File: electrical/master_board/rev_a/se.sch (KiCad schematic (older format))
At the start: 0 parts

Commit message: Added spacer mounting holes to schematics and associated PCB's.
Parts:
- added H3: HOLE;M2.5, MountingHole:MountingHole_2.7mm_M2.5, symbol HR2:HOLE;M2.5
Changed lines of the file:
@@
 Comment4 ""
 $EndDescr
+$Comp
+L HR2:HOLE;M2.5 H3
+U 1 1 5F2F795F
+P 3200 4100
+F 0 "H3" H 3150 4150 60  0000 L CNN
+F 1 "HOLE;M2.5" H 3000 4050 60  0000 L CNN
+F 2 "MountingHole:MountingHole_2.7mm_M2.5" H 3400 4150 60  0001 L CNN
+F 3 "M2.5 Mounting Hole" H 3400 3950 60  0001 L CNN
+	1    3200 4100
+	1    0    0    -1
+$EndComp
 $EndSCHEMATC

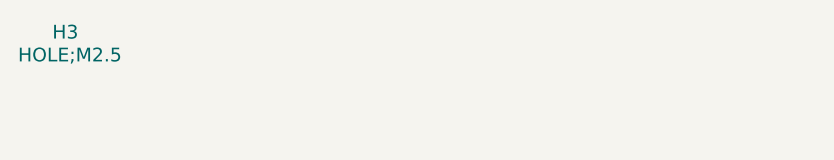
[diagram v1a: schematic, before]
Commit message: Added LED's to the PCB's.
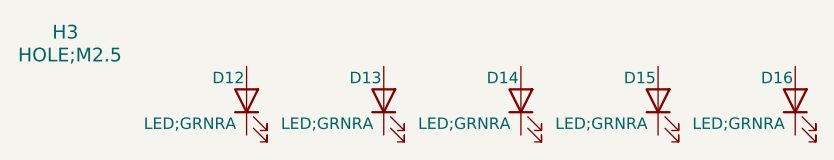
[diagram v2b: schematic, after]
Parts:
- added D12, D13, D14, D15, D16: LED;GRNRA, HR2:LED_GRNRA, symbol Device:LED
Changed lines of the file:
@@
 	1    0    0    -1
 $EndComp
+$Comp
+L Device:LED D12
+U 1 1 5F30C7E5
+P 4000 4350
+F 0 "D12" V 4100 4500 50  0000 R CNN
+F 1 "LED;GRNRA" V 3900 4800 50  0000 R CNN
+F 2 "HR2:LED_GRNRA" H 4000 4350 50  0001 C CNN
+F 3 "~" H 4000 4350 50  0001 C CNN
+	1    4000 4350
+	0    -1   -1   0
+$EndComp
+$Comp
+L Device:LED D14
+U 1 1 5F30E8C7
+P 5200 4350
+F 0 "D14" V 5300 4500 50  0000 R CNN
+F 1 "LED;GRNRA" V 5100 4800 50  0000 R CNN
+F 2 "HR2:LED_GRNRA" H 5200 4350 50  0001 C CNN
+F 3 "~" H 5200 4350 50  0001 C CNN
+	1    5200 4350
+	0    -1   -1   0
+$EndComp
+$Comp
+L Device:LED D15
+U 1 1 5F30E8D1
+P 5800 4350
+F 0 "D15" V 5900 4500 50  0000 R CNN
+F 1 "LED;GRNRA" V 5700 4800 50  0000 R CNN
+F 2 "HR2:LED_GRNRA" H 5800 4350 50  0001 C CNN
+F 3 "~" H 5800 4350 50  0001 C CNN
+	1    5800 4350
+	0    -1   -1   0
+$EndComp
+$Comp
+L Device:LED D16
+U 1 1 5F30F503
+P 6400 4350
+F 0 "D16" V 6500 4500 50  0000 R CNN
+F 1 "LED;GRNRA" V 6300 4800 50  0000 R CNN
+F 2 "HR2:LED_GRNRA" H 6400 4350 50  0001 C CNN
+F 3 "~" H 6400 4350 50  0001 C CNN
+	1    6400 4350
+	0    -1   -1   0
+$EndComp
+$Comp
+L Device:LED D13
+U 1 1 5F30E2EA
+P 4600 4350
+F 0 "D13" V 4700 4500 50  0000 R CNN
+F 1 "LED;GRNRA" V 4500 4800 50  0000 R CNN
+F 2 "HR2:LED_GRNRA" H 4600 4350 50  0001 C CNN
+F 3 "~" H 4600 4350 50  0001 C CNN
+	1    4600 4350
+	0    -1   -1   0
+$EndComp
 $EndSCHEMATC

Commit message: Got Bridge connectors installed on PCB's. Tweaking still required.
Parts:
- added CN107: BRIDGE_SE_OUTER;M1x8, HR2:BRIDGE_SE_OUTER_M1x8, symbol HR2:BRIDGE_SE_OUTER;M1x8
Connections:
- no-connect marks 0 -> 8
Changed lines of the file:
@@
 	0    -1   -1   0
 $EndComp
+$Comp
+L HR2:BRIDGE_SE_OUTER;M1x8 CN107
+U 1 1 5F387B22
+P 3400 2300
+F 0 "CN107" H 3700 2450 50  0000 C CNN
+F 1 "BRIDGE_SE_OUTER;M1x8" H 3750 1450 50  0000 C CNN
+F 2 "HR2:BRIDGE_SE_OUTER_M1x8" H 3600 2350 60  0001 L CNN
+F 3 "" H 3600 2150 60  0001 L CNN
+F 4 "SE Outer Bridge Connector" H 3600 2050 60  0001 L CNN "Field5"
+	1    3400 2300
+	1    0    0    -1
+$EndComp
+NoConn ~ 4100 2300
+NoConn ~ 4100 2400
+NoConn ~ 4100 2500
+NoConn ~ 4100 2600
+NoConn ~ 4100 2700
+NoConn ~ 4100 2800
+NoConn ~ 4100 2900
+NoConn ~ 4100 3000
 $EndSCHEMATC

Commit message: The four corner boards ne/nw/se/sw are now zoned.
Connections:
- net labels added: GND
- wire segments 0 -> 1
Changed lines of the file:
@@
 	1    0    0    -1
 $EndComp
-NoConn ~ 4100 2300
 NoConn ~ 4100 2400
 NoConn ~ 4100 2500
@@
 NoConn ~ 4100 2900
 NoConn ~ 4100 3000
+Wire Wire Line
+	4100 2300 4500 2300
+NoConn ~ 4500 2300
+Text Label 4200 2300 0    50   ~ 0
+GND
 $EndSCHEMATC

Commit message: Positioned all of the parts on SW board.
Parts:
- added Q12, Q13, Q14, Q15, Q16: 2N7000;SOT23, Package_TO_SOT_SMD:SOT-23, symbol Transistor_FET:2N7000
- added R36, R37, R38, R39, R40, R41, R42, R43, R44, R45, R46, R47, R48, R49, R50: 330;1608, Resistor_SMD:R_0603_1608Metric, symbol Device:R_US
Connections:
- net labels added: 9V, LED12, LED13, LED14, LED15, LED16
- wire segments 1 -> 97
- no-connect marks 8 -> 1
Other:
- note added: "Note: GRNRA = Green Right Angle 0.254mm (approx.) lead spacing"
- note added: "Note: LED's are labeled from 1 to 16 in a clockwise\ndirection starting in the NW quadrant near the X axis."
- note added: "Note: Mounting Hole for above\narm expansion plates."
- note added: "Right Angle Green LED\nMfg Part #: TLPG5600\nDigi-Key part #: TLPG5600-ND\nForward Voltage Drop: 2.4V\nAbsolute max. current: 200mA\nTarget current: I=60mA\nR = (9V - 2.4V) / 75mA = 6.6V / .060A = 110Ohm\nW=I**2*R = (.060 * .060) * 110=.495W = .396W =.4W\nUse 3 330Ohm resistors in parallel to get 110Ohm\n1/8 Watt or larger should work.\n\n.\n"

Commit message: Got NE PCB done.
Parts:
- R36, R37, R38, R39, R40, R41, R42, R43, R44, R45, R46, R47, R48, R49, R50: value 330;1608 -> 330Ω;1608
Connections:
- no-connect marks 1 -> 2
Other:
- note added: "Notes:\n1. GRNRA = Green Right Angle Green\n2. Nominal Part:\n Mfg Part #: TLPG5600\n Digi-Key part #: TLPG5600-ND\n Forward Voltage Drop: 2.4V\n Absolute max. current: 200mA\n Target maximum current: I=60mA\n Resistor: R = (9V - 2.4V) / 75mA = 6.6V / .060A = 110Ω\n Watts: W = I**2*R = (.060 * .060) * 110 = .396W ~=.4W\n Use 3 x 330Ω in parallel to get 110Ω\n Watts per resistor: Wr = .4W / 3 = .1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"
- note removed: "Note: GRNRA = Green Right Angle 0.254mm (approx.) lead spacing"
- note removed: "Right Angle Green LED\nMfg Part #: TLPG5600\nDigi-Key part #: TLPG5600-ND\nForward Voltage Drop: 2.4V\nAbsolute max. current: 200mA\nTarget current: I=60mA\nR = (9V - 2.4V) / 75mA = 6.6V / .060A = 110Ohm\nW=I**2*R = (.060 * .060) * 110=.495W = .396W =.4W\nUse 3 330Ohm resistors in parallel to get 110Ohm\n1/8 Watt or larger should work.\n\n.\n"
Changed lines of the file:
@@
 	0    -1   -1   0
 $EndComp
-NoConn ~ 3250 1950
 Wire Wire Line
 	8050 4550 8050 4450
@@
 AR Path="/5F3FF723" Ref="R37"  Part="1"
 F 0 "R37" V 7700 3050 50  0000 L CNN
-F 1 "330;1608" V 7900 2950 50  0000 L CNN
+F 1 "330Ω;1608" V 7900 2950 50  0000 L CNN
 F 2 "Resistor_SMD:R_0603_1608Metric" V 7840 3140 50  0001 C CNN
 F 3 "~" H 7800 3150 50  0001 C CNN
@@
 $EndComp
 Text Notes 2750 6100 0    50   ~ 0
-Right Angle Green LED\nMfg Part #: TLPG5600\nDigi-Key part #: TLPG5600-ND\nForward Voltage Drop: 2.4V\nAbsolute max. current: 200mA\nTarget current: I=60mA\nR = (9V - 2.4V) / 75mA = 6.6V / .060A = 110Ohm\nW=I**2*R = (.060 * .060) * 110=.495W = .396W =.4W\nUse 3 330Ohm resistors in parallel to get 110Ohm\n1/8 Watt or larger should work.\n\n.\n
+Notes:\n1. GRNRA = Green Right Angle Green\n2. Nominal Part:\n     Mfg Part #: TLPG5600\n     Digi-Key part #: TLPG5600-ND\n     Forward Voltage Drop: 2.4V\n     Absolute max. current: 200mA\n     Target maximum current: I=60mA\n     Resistor: R = (9V - 2.4V) / 75mA = 6.6V / .060A = 110Ω\n     Watts: W = I**2*R = (.060 * .060) * 110 = .396W ~=.4W\n     Use 3 x 330Ω in parallel to get 110Ω\n     Watts per resistor: Wr = .4W / 3 = .133W ~= .125W\n     1/8W or larger should work.\n3. LED's are labeled from 1 to 16 in a counter-clockwise\n     direction starting in the NW quadrant nearest the X axis.
 Wire Wire Line
 	8050 4050 8050 3950
@@
 AR Path="/5F3FF72B" Ref="R38"  Part="1"
 F 0 "R38" V 7700 2750 50  0000 L CNN
-F 1 "330;1608" V 7900 2650 50  0000 L CNN
+F 1 "330Ω;1608" V 7900 2650 50  0000 L CNN
 F 2 "Resistor_SMD:R_0603_1608Metric" V 7840 2840 50  0001 C CNN
 F 3 "~" H 7800 2850 50  0001 C CNN
@@
 AR Path="/5F3FF731" Ref="R36"  Part="1"
 F 0 "R36" V 7700 3350 50  0000 L CNN
-F 1 "330;1608" V 7900 3250 50  0000 L CNN
+F 1 "330Ω;1608" V 7900 3250 50  0000 L CNN
 F 2 "Resistor_SMD:R_0603_1608Metric" V 7840 3440 50  0001 C CNN
 F 3 "~" H 7800 3450 50  0001 C CNN
@@
 AR Path="/5F3FF74C" Ref="R40"  Part="1"
 F 0 "R40" V 6800 3050 50  0000 L CNN
-F 1 "330;1608" V 7000 2950 50  0000 L CNN
+F 1 "330Ω;1608" V 7000 2950 50  0000 L CNN
 F 2 "Resistor_SMD:R_0603_1608Metric" V 6940 3140 50  0001 C CNN
 F 3 "~" H 6900 3150 50  0001 C CNN
@@
 AR Path="/5F3FF753" Ref="R41"  Part="1"
 F 0 "R41" V 6800 2750 50  0000 L CNN
-F 1 "330;1608" V 7000 2650 50  0000 L CNN
+F 1 "330Ω;1608" V 7000 2650 50  0000 L CNN
 F 2 "Resistor_SMD:R_0603_1608Metric" V 6940 2840 50  0001 C CNN
 F 3 "~" H 6900 2850 50  0001 C CNN
@@
 AR Path="/5F3FF759" Ref="R39"  Part="1"
 F 0 "R39" V 6800 3350 50  0000 L CNN
-F 1 "330;1608" V 7000 3250 50  0000 L CNN
+F 1 "330Ω;1608" V 7000 3250 50  0000 L CNN
 F 2 "Resistor_SMD:R_0603_1608Metric" V 6940 3440 50  0001 C CNN
 F 3 "~" H 6900 3450 50  0001 C CNN
@@
 AR Path="/5F3FF77A" Ref="R46"  Part="1"
 F 0 "R46" V 5000 3050 50  0000 L CNN
-F 1 "330;1608" V 5200 2950 50  0000 L CNN
+F 1 "330Ω;1608" V 5200 2950 50  0000 L CNN
 F 2 "Resistor_SMD:R_0603_1608Metric" V 5140 3140 50  0001 C CNN
 F 3 "~" H 5100 3150 50  0001 C CNN
@@
 AR Path="/5F3FF781" Ref="R47"  Part="1"
 F 0 "R47" V 5000 2750 50  0000 L CNN
-F 1 "330;1608" V 5200 2650 50  0000 L CNN
+F 1 "330Ω;1608" V 5200 2650 50  0000 L CNN
 F 2 "Resistor_SMD:R_0603_1608Metric" V 5140 2840 50  0001 C CNN
 F 3 "~" H 5100 2850 50  0001 C CNN
@@
 AR Path="/5F3FF787" Ref="R45"  Part="1"
 F 0 "R45" V 5000 3350 50  0000 L CNN
-F 1 "330;1608" V 5200 3250 50  0000 L CNN
+F 1 "330Ω;1608" V 5200 3250 50  0000 L CNN
 F 2 "Resistor_SMD:R_0603_1608Metric" V 5140 3440 50  0001 C CNN
 F 3 "~" H 5100 3450 50  0001 C CNN
@@
 AR Path="/5F3FF7A2" Ref="R49"  Part="1"
 F 0 "R49" V 4100 3050 50  0000 L CNN
-F 1 "330;1608" V 4300 2950 50  0000 L CNN
+F 1 "330Ω;1608" V 4300 2950 50  0000 L CNN
 F 2 "Resistor_SMD:R_0603_1608Metric" V 4240 3140 50  0001 C CNN
 F 3 "~" H 4200 3150 50  0001 C CNN
@@
 AR Path="/5F3FF7A8" Ref="R50"  Part="1"
 F 0 "R50" V 4100 2750 50  0000 L CNN
-F 1 "330;1608" V 4300 2650 50  0000 L CNN
+F 1 "330Ω;1608" V 4300 2650 50  0000 L CNN
 F 2 "Resistor_SMD:R_0603_1608Metric" V 4240 2840 50  0001 C CNN
 F 3 "~" H 4200 2850 50  0001 C CNN
@@
 AR Path="/5F3FF7AE" Ref="R48"  Part="1"
 F 0 "R48" V 4100 3350 50  0000 L CNN
-F 1 "330;1608" V 4300 3250 50  0000 L CNN
+F 1 "330Ω;1608" V 4300 3250 50  0000 L CNN
 F 2 "Resistor_SMD:R_0603_1608Metric" V 4240 3440 50  0001 C CNN
 F 3 "~" H 4200 3450 50  0001 C CNN
@@
 Wire Wire Line
 	3250 2550 3850 2550
-Wire Wire Line
-	3250 2650 3550 2650
 Wire Wire Line
 	8050 4550 7150 4550
@@
 AR Path="/5F3FF7D7" Ref="R42"  Part="1"
 F 0 "R42" V 5900 3350 50  0000 L CNN
-F 1 "330;1608" V 6100 3250 50  0000 L CNN
+F 1 "330Ω;1608" V 6100 3250 50  0000 L CNN
 F 2 "Resistor_SMD:R_0603_1608Metric" V 6040 3440 50  0001 C CNN
 F 3 "~" H 6000 3450 50  0001 C CNN
@@
 AR Path="/5F3FF7DD" Ref="R44"  Part="1"
 F 0 "R44" V 5900 2750 50  0000 L CNN
-F 1 "330;1608" V 6100 2650 50  0000 L CNN
+F 1 "330Ω;1608" V 6100 2650 50  0000 L CNN
 F 2 "Resistor_SMD:R_0603_1608Metric" V 6040 2840 50  0001 C CNN
 F 3 "~" H 6000 2850 50  0001 C CNN
@@
 AR Path="/5F3FF7E4" Ref="R43"  Part="1"
 F 0 "R43" V 5900 3050 50  0000 L CNN
-F 1 "330;1608" V 6100 2950 50  0000 L CNN
+F 1 "330Ω;1608" V 6100 2950 50  0000 L CNN
 F 2 "Resistor_SMD:R_0603_1608Metric" V 6040 3140 50  0001 C CNN
 F 3 "~" H 6000 3150 50  0001 C CNN
@@
 Wire Wire Line
 	4450 4550 3550 4550
-Wire Wire Line
-	3550 4550 3550 2650
 Connection ~ 4450 4550
 Connection ~ 5350 4550
@@
 Text Label 7500 4250 0    50   ~ 0
 LED12
-Text Label 3300 2650 0    50   ~ 0
+Text Label 3300 1950 0    50   ~ 0
 GND
 Text Label 3650 2050 0    50   ~ 0
 9V
-Text Notes 2750 6500 0    50   ~ 0
-Note: GRNRA = Green Right Angle 0.254mm (approx.) lead spacing
 Text Notes 2750 6250 0    50   ~ 0
 Note: LED's are labeled from 1 to 16 in a clockwise\ndirection starting in the NW quadrant near the X axis.
@@
 Wire Wire Line
 	7450 2150 7450 4250
+Wire Wire Line
+	3550 4550 3550 1950
+Wire Wire Line
+	3550 1950 3250 1950
+NoConn ~ 3250 2650
+NoConn ~ 1500 1800
 $EndSCHEMATC

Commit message: Linked the NE/NW/SE/SW sheets to master_board.
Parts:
- renumbered CN107 to CN?
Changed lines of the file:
@@
 $Descr A 11000 8500
 encoding utf-8
-Sheet 1 1
+Sheet 10 12
 Title "HR2 SE PCB"
 Date "2020-06-13"
@@
 AR Path="/5F3DFBDE/5F3FF6FB" Ref="H?"  Part="1"
 AR Path="/5F3FF6FB" Ref="H3"  Part="1"
-F 0 "H3" H 2550 4150 50  0000 L CNN
+AR Path="/5F79E273/5F3FF6FB" Ref="H?"  Part="1"
+F 0 "H?" H 2550 4150 50  0000 L CNN
 F 1 "HOLE;M2.5" H 2400 4050 50  0000 L CNN
 F 2 "MountingHole:MountingHole_2.7mm_M2.5" H 2800 4150 60  0001 L CNN
@@
 AR Path="/5F3DFBDE/5F3FF701" Ref="D?"  Part="1"
 AR Path="/5F3FF701" Ref="D15"  Part="1"
-F 0 "D15" V 5450 3950 50  0000 R CNN
+AR Path="/5F79E273/5F3FF701" Ref="D?"  Part="1"
+F 0 "D?" V 5450 3950 50  0000 R CNN
 F 1 "LED;GRNRA" V 5250 4250 50  0000 R CNN
 F 2 "HR2:LED_GRNRA" H 5350 3800 50  0001 C CNN
@@
 AR Path="/5F3DFBDE/5F3FF707" Ref="D?"  Part="1"
 AR Path="/5F3FF707" Ref="D13"  Part="1"
-F 0 "D13" V 7250 3950 50  0000 R CNN
+AR Path="/5F79E273/5F3FF707" Ref="D?"  Part="1"
+F 0 "D?" V 7250 3950 50  0000 R CNN
 F 1 "LED;GRNRA" V 7050 4250 50  0000 R CNN
 F 2 "HR2:LED_GRNRA" H 7150 3800 50  0001 C CNN
@@
 AR Path="/5F3DFBDE/5F3FF70D" Ref="D?"  Part="1"
 AR Path="/5F3FF70D" Ref="D12"  Part="1"
-F 0 "D12" V 8150 3950 50  0000 R CNN
+AR Path="/5F79E273/5F3FF70D" Ref="D?"  Part="1"
+F 0 "D?" V 8150 3950 50  0000 R CNN
 F 1 "LED;GRNRA" V 7950 4250 50  0000 R CNN
 F 2 "HR2:LED_GRNRA" H 8050 3800 50  0001 C CNN
@@
 AR Path="/5F3DFBDE/5F3FF71D" Ref="Q?"  Part="1"
 AR Path="/5F3FF71D" Ref="Q12"  Part="1"
-F 0 "Q12" H 7800 4400 50  0000 L CNN
+AR Path="/5F79E273/5F3FF71D" Ref="Q?"  Part="1"
+F 0 "Q?" H 7800 4400 50  0000 L CNN
 F 1 "2N7000;SOT23" H 7350 4200 50  0000 L CNN
 F 2 "Package_TO_SOT_SMD:SOT-23" H 8150 4175 50  0001 L CIN
@@
 AR Path="/5F3DFBDE/5F3FF723" Ref="R?"  Part="1"
 AR Path="/5F3FF723" Ref="R37"  Part="1"
-F 0 "R37" V 7700 3050 50  0000 L CNN
+AR Path="/5F79E273/5F3FF723" Ref="R?"  Part="1"
+F 0 "R?" V 7700 3050 50  0000 L CNN
 F 1 "330Ω;1608" V 7900 2950 50  0000 L CNN
 F 2 "Resistor_SMD:R_0603_1608Metric" V 7840 3140 50  0001 C CNN
@@
 AR Path="/5F3DFBDE/5F3FF72B" Ref="R?"  Part="1"
 AR Path="/5F3FF72B" Ref="R38"  Part="1"
-F 0 "R38" V 7700 2750 50  0000 L CNN
+AR Path="/5F79E273/5F3FF72B" Ref="R?"  Part="1"
+F 0 "R?" V 7700 2750 50  0000 L CNN
 F 1 "330Ω;1608" V 7900 2650 50  0000 L CNN
 F 2 "Resistor_SMD:R_0603_1608Metric" V 7840 2840 50  0001 C CNN
@@
 AR Path="/5F3DFBDE/5F3FF731" Ref="R?"  Part="1"
 AR Path="/5F3FF731" Ref="R36"  Part="1"
-F 0 "R36" V 7700 3350 50  0000 L CNN
+AR Path="/5F79E273/5F3FF731" Ref="R?"  Part="1"
+F 0 "R?" V 7700 3350 50  0000 L CNN
 F 1 "330Ω;1608" V 7900 3250 50  0000 L CNN
 F 2 "Resistor_SMD:R_0603_1608Metric" V 7840 3440 50  0001 C CNN
@@
 AR Path="/5F3DFBDE/5F3FF746" Ref="Q?"  Part="1"
 AR Path="/5F3FF746" Ref="Q13"  Part="1"
-F 0 "Q13" H 6900 4400 50  0000 L CNN
+AR Path="/5F79E273/5F3FF746" Ref="Q?"  Part="1"
+F 0 "Q?" H 6900 4400 50  0000 L CNN
 F 1 "2N7000;SOT23" H 6450 4200 50  0000 L CNN
 F 2 "Package_TO_SOT_SMD:SOT-23" H 7250 4175 50  0001 L CIN
@@
 AR Path="/5F3DFBDE/5F3FF74C" Ref="R?"  Part="1"
 AR Path="/5F3FF74C" Ref="R40"  Part="1"
-F 0 "R40" V 6800 3050 50  0000 L CNN
+AR Path="/5F79E273/5F3FF74C" Ref="R?"  Part="1"
+F 0 "R?" V 6800 3050 50  0000 L CNN
 F 1 "330Ω;1608" V 7000 2950 50  0000 L CNN
 F 2 "Resistor_SMD:R_0603_1608Metric" V 6940 3140 50  0001 C CNN
@@
 AR Path="/5F3DFBDE/5F3FF753" Ref="R?"  Part="1"
 AR Path="/5F3FF753" Ref="R41"  Part="1"
-F 0 "R41" V 6800 2750 50  0000 L CNN
+AR Path="/5F79E273/5F3FF753" Ref="R?"  Part="1"
+F 0 "R?" V 6800 2750 50  0000 L CNN
 F 1 "330Ω;1608" V 7000 2650 50  0000 L CNN
 F 2 "Resistor_SMD:R_0603_1608Metric" V 6940 2840 50  0001 C CNN
@@
 AR Path="/5F3DFBDE/5F3FF759" Ref="R?"  Part="1"
 AR Path="/5F3FF759" Ref="R39"  Part="1"
-F 0 "R39" V 6800 3350 50  0000 L CNN
+AR Path="/5F79E273/5F3FF759" Ref="R?"  Part="1"
+F 0 "R?" V 6800 3350 50  0000 L CNN
 F 1 "330Ω;1608" V 7000 3250 50  0000 L CNN
 F 2 "Resistor_SMD:R_0603_1608Metric" V 6940 3440 50  0001 C CNN
@@
 AR Path="/5F3DFBDE/5F3FF774" Ref="Q?"  Part="1"
 AR Path="/5F3FF774" Ref="Q15"  Part="1"
-F 0 "Q15" H 5100 4400 50  0000 L CNN
+AR Path="/5F79E273/5F3FF774" Ref="Q?"  Part="1"
+F 0 "Q?" H 5100 4400 50  0000 L CNN
 F 1 "2N7000;SOT23" H 4650 4200 50  0000 L CNN
 F 2 "Package_TO_SOT_SMD:SOT-23" H 5450 4175 50  0001 L CIN
@@
 AR Path="/5F3DFBDE/5F3FF77A" Ref="R?"  Part="1"
 AR Path="/5F3FF77A" Ref="R46"  Part="1"
-F 0 "R46" V 5000 3050 50  0000 L CNN
+AR Path="/5F79E273/5F3FF77A" Ref="R?"  Part="1"
+F 0 "R?" V 5000 3050 50  0000 L CNN
 F 1 "330Ω;1608" V 5200 2950 50  0000 L CNN
 F 2 "Resistor_SMD:R_0603_1608Metric" V 5140 3140 50  0001 C CNN
@@
 AR Path="/5F3DFBDE/5F3FF781" Ref="R?"  Part="1"
 AR Path="/5F3FF781" Ref="R47"  Part="1"
-F 0 "R47" V 5000 2750 50  0000 L CNN
+AR Path="/5F79E273/5F3FF781" Ref="R?"  Part="1"
+F 0 "R?" V 5000 2750 50  0000 L CNN
 F 1 "330Ω;1608" V 5200 2650 50  0000 L CNN
 F 2 "Resistor_SMD:R_0603_1608Metric" V 5140 2840 50  0001 C CNN
@@
 AR Path="/5F3DFBDE/5F3FF787" Ref="R?"  Part="1"
 AR Path="/5F3FF787" Ref="R45"  Part="1"
-F 0 "R45" V 5000 3350 50  0000 L CNN
+AR Path="/5F79E273/5F3FF787" Ref="R?"  Part="1"
+F 0 "R?" V 5000 3350 50  0000 L CNN
 F 1 "330Ω;1608" V 5200 3250 50  0000 L CNN
 F 2 "Resistor_SMD:R_0603_1608Metric" V 5140 3440 50  0001 C CNN
@@
 AR Path="/5F3DFBDE/5F3FF79C" Ref="Q?"  Part="1"
 AR Path="/5F3FF79C" Ref="Q16"  Part="1"
-F 0 "Q16" H 4200 4400 50  0000 L CNN
+AR Path="/5F79E273/5F3FF79C" Ref="Q?"  Part="1"
+F 0 "Q?" H 4200 4400 50  0000 L CNN
 F 1 "2N7000;SOT23" H 3750 4200 50  0000 L CNN
 F 2 "Package_TO_SOT_SMD:SOT-23" H 4550 4175 50  0001 L CIN
@@
 AR Path="/5F3DFBDE/5F3FF7A2" Ref="R?"  Part="1"
 AR Path="/5F3FF7A2" Ref="R49"  Part="1"
-F 0 "R49" V 4100 3050 50  0000 L CNN
+AR Path="/5F79E273/5F3FF7A2" Ref="R?"  Part="1"
+F 0 "R?" V 4100 3050 50  0000 L CNN
 F 1 "330Ω;1608" V 4300 2950 50  0000 L CNN
 F 2 "Resistor_SMD:R_0603_1608Metric" V 4240 3140 50  0001 C CNN
@@
 AR Path="/5F3DFBDE/5F3FF7A8" Ref="R?"  Part="1"
 AR Path="/5F3FF7A8" Ref="R50"  Part="1"
-F 0 "R50" V 4100 2750 50  0000 L CNN
+AR Path="/5F79E273/5F3FF7A8" Ref="R?"  Part="1"
+F 0 "R?" V 4100 2750 50  0000 L CNN
 F 1 "330Ω;1608" V 4300 2650 50  0000 L CNN
 F 2 "Resistor_SMD:R_0603_1608Metric" V 4240 2840 50  0001 C CNN
@@
 AR Path="/5F3DFBDE/5F3FF7AE" Ref="R?"  Part="1"
 AR Path="/5F3FF7AE" Ref="R48"  Part="1"
-F 0 "R48" V 4100 3350 50  0000 L CNN
+AR Path="/5F79E273/5F3FF7AE" Ref="R?"  Part="1"
+F 0 "R?" V 4100 3350 50  0000 L CNN
 F 1 "330Ω;1608" V 4300 3250 50  0000 L CNN
 F 2 "Resistor_SMD:R_0603_1608Metric" V 4240 3440 50  0001 C CNN
@@
 AR Path="/5F3DFBDE/5F3FF7C8" Ref="D?"  Part="1"
 AR Path="/5F3FF7C8" Ref="D16"  Part="1"
-F 0 "D16" V 4550 3950 50  0000 R CNN
+AR Path="/5F79E273/5F3FF7C8" Ref="D?"  Part="1"
+F 0 "D?" V 4550 3950 50  0000 R CNN
 F 1 "LED;GRNRA" V 4350 4250 50  0000 R CNN
 F 2 "HR2:LED_GRNRA" H 4450 3800 50  0001 C CNN
@@
 AR Path="/5F3DFBDE/5F3FF7D7" Ref="R?"  Part="1"
 AR Path="/5F3FF7D7" Ref="R42"  Part="1"
-F 0 "R42" V 5900 3350 50  0000 L CNN
+AR Path="/5F79E273/5F3FF7D7" Ref="R?"  Part="1"
+F 0 "R?" V 5900 3350 50  0000 L CNN
 F 1 "330Ω;1608" V 6100 3250 50  0000 L CNN
 F 2 "Resistor_SMD:R_0603_1608Metric" V 6040 3440 50  0001 C CNN
@@
 AR Path="/5F3DFBDE/5F3FF7DD" Ref="R?"  Part="1"
 AR Path="/5F3FF7DD" Ref="R44"  Part="1"
-F 0 "R44" V 5900 2750 50  0000 L CNN
+AR Path="/5F79E273/5F3FF7DD" Ref="R?"  Part="1"
+F 0 "R?" V 5900 2750 50  0000 L CNN
 F 1 "330Ω;1608" V 6100 2650 50  0000 L CNN
 F 2 "Resistor_SMD:R_0603_1608Metric" V 6040 2840 50  0001 C CNN
@@
 AR Path="/5F3DFBDE/5F3FF7E4" Ref="R?"  Part="1"
 AR Path="/5F3FF7E4" Ref="R43"  Part="1"
-F 0 "R43" V 5900 3050 50  0000 L CNN
+AR Path="/5F79E273/5F3FF7E4" Ref="R?"  Part="1"
+F 0 "R?" V 5900 3050 50  0000 L CNN
 F 1 "330Ω;1608" V 6100 2950 50  0000 L CNN
 F 2 "Resistor_SMD:R_0603_1608Metric" V 6040 3140 50  0001 C CNN
@@
 AR Path="/5F3DFBDE/5F3FF7EA" Ref="Q?"  Part="1"
 AR Path="/5F3FF7EA" Ref="Q14"  Part="1"
-F 0 "Q14" H 6000 4400 50  0000 L CNN
+AR Path="/5F79E273/5F3FF7EA" Ref="Q?"  Part="1"
+F 0 "Q?" H 6000 4400 50  0000 L CNN
 F 1 "2N7000;SOT23" H 5550 4200 50  0000 L CNN
 F 2 "Package_TO_SOT_SMD:SOT-23" H 6350 4175 50  0001 L CIN
@@
 AR Path="/5F3DFBDE/5F3FF7F1" Ref="D?"  Part="1"
 AR Path="/5F3FF7F1" Ref="D14"  Part="1"
-F 0 "D14" V 6350 3950 50  0000 R CNN
+AR Path="/5F79E273/5F3FF7F1" Ref="D?"  Part="1"
+F 0 "D?" V 6350 3950 50  0000 R CNN
 F 1 "LED;GRNRA" V 6150 4250 50  0000 R CNN
 F 2 "HR2:LED_GRNRA" H 6250 3800 50  0001 C CNN
@@
 	4150 4250 3850 4250
 $Comp
-L HR2:BRIDGE_SE_OUTER;M1x8 CN107
+L HR2:BRIDGE_SE_OUTER;M1x8 CN?
 U 1 1 5F41FB8B
 P 2450 1950
-F 0 "CN107" H 2956 2240 60  0000 C CNN
+F 0 "CN?" H 2956 2240 60  0000 C CNN
 F 1 "BRIDGE_SE_OUTER;M1x8" H 2956 2134 60  0000 C CNN
 F 2 "HR2:BRIDGE_SE_OUTER_M1x8" H 2650 2000 60  0001 L CNN

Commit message: Reworked Sonars, Servers, and LED's schematics.
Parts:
- removed CN?: BRIDGE_SE_OUTER;M1x8, HR2:BRIDGE_SE_OUTER_M1x8, symbol HR2:BRIDGE_SE_OUTER;M1x8
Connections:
- wire segments 97 -> 95
- no-connect marks 2 -> 1
